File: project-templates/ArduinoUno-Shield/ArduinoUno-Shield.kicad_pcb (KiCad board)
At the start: 2 copper layers, 68.8 x 53.3 mm, 1 part

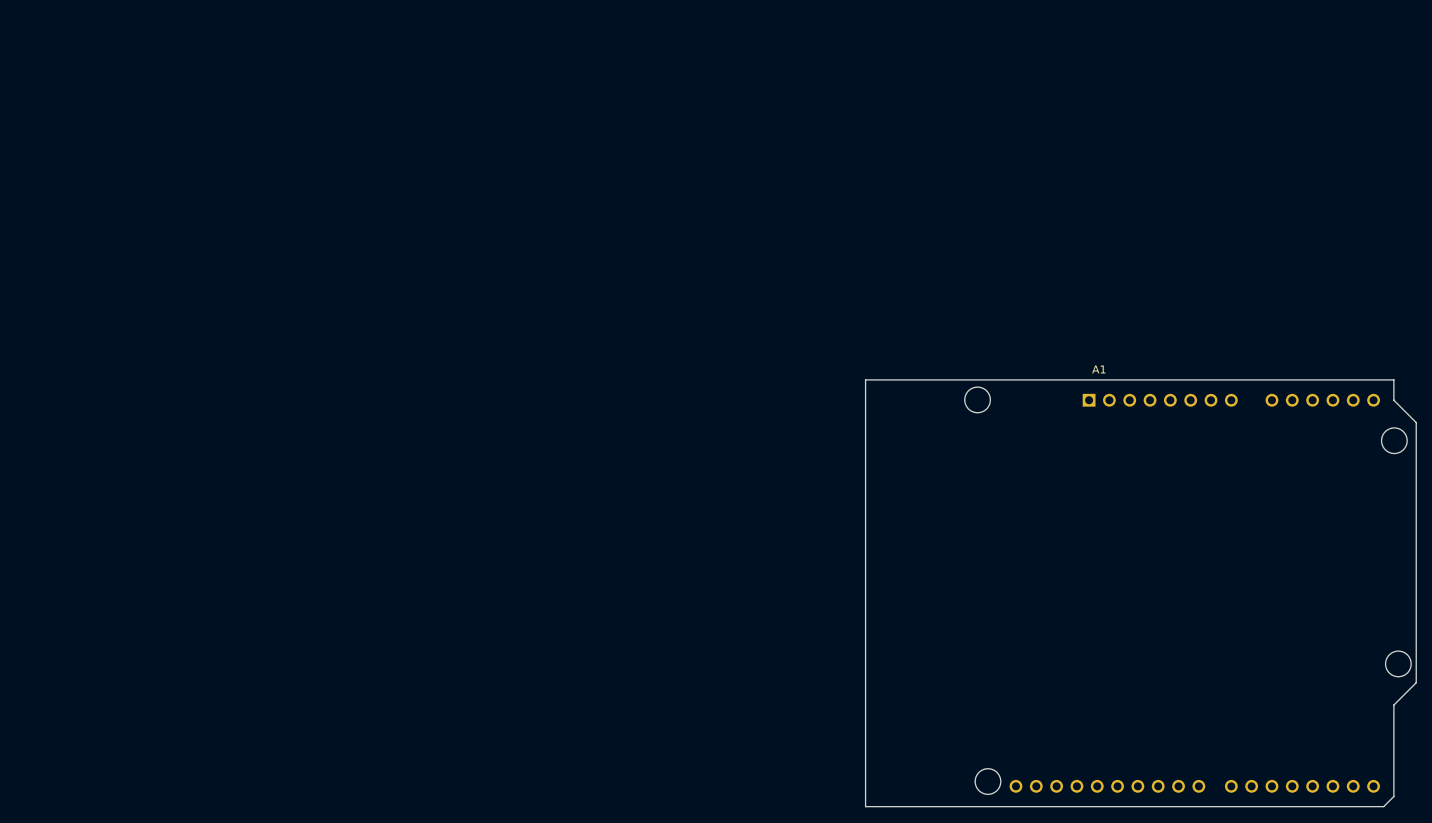
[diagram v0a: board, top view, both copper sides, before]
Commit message: Fixed Arduino footprint orientation (top/bottom)
Arduino shield PCB now expects to be mounted on top of an Arduino,
i.e. the Arduino footprint is on the bottom
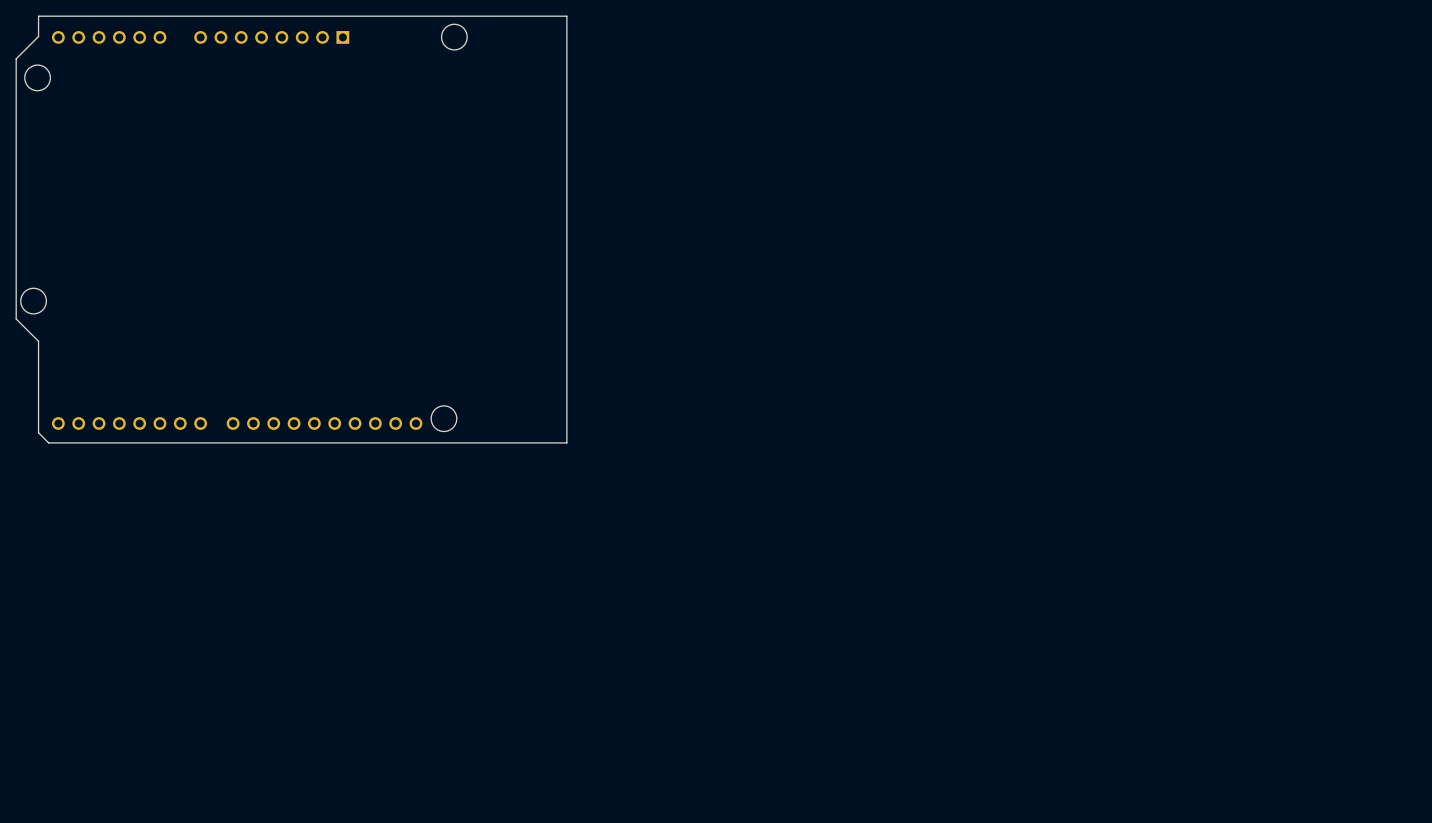
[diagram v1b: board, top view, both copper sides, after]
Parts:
- A1: moved to B.Cu
- moved A1 58.8 mm to (98.0, 26.3), turned to 180 degrees
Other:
- outline, holes or cut-outs redrawn
